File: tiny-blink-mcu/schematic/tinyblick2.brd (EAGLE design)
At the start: 35 x 35 mm, 57 parts, among them IC1 SE555D, IC2 LM358D, IC3 74LS595D, IC4 74LS595D, J1 USB-MICROB

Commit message: Updated schematic and board layout
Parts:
- removed C3: 10nF, adafruit:C0603
- removed C4: 100nF, adafruit:C0603
- removed C6: 5nF, adafruit:C0603
- removed C7: 0uF, adafruit:C0603
- removed C9: 4.7uF, adafruit:C0603
- removed IC1: SE555D, adafruit:SO08
- removed IC2: LM358D, linear:SO08
- removed R10: 10K, adafruit:R0603
- removed R11: 1K, adafruit:R0603
- removed R12: 5.1K, adafruit:R0603
- added C12: 10nF, adafruit:C0603
- added S1: MOMENTARY-SWITCH-SPST-SMD-4.6X2.8MM, SparkFun-Switches:TACTILE_SWITCH_SMD_4.6X2.8MM
- added TP1, TP2, TP3, TP4, TP5, TP6: TPB1,27, testpad:B1,27
- R1: value 10K -> (none)
- moved R1 13.6 mm to (6.50, 23.5), turned to 270 degrees
- moved C10 7.52 mm to (17.8, 31.3), turned to 180 degrees
- moved U$2 4.30 mm to (17.7, 27.7), turned to 270 degrees
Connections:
- removed net CLR: IC3.12, IC4.12, U$2.2
- removed net N$26: IC2.3, R1.1, R10.2
- removed net N$3: IC1.7, R11.1, R12.2
- removed net N$30: C6.2, IC1.5
- removed net N$6: C7.1, C9.1, IC1.2, IC1.6, R12.1
- new net LATCH: C12.2, IC3.12, IC4.12, TP1.TP, U$2.2
- new net NRES: TP3.TP, U$2.1
- new net PB4: R1.1, S1.3, S1.4, TP2.TP, U$2.3
- net +3V3: no longer C3.1, C4.1, IC1.4, IC1.8, IC2.8, R11.2
- net CLK: no longer IC1.3, IC2.2
- net GND: now also C12.1, S1.1, S1.2; no longer C3.2, C4.2, C6.1, C7.2, C9.2, IC1.1, IC2.4, R10.1
- net PWM: now also TP6.TP
- net RCLK: now also TP5.TP; no longer IC2.1
- net SER: now also TP4.TP
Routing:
- net +3V3: track 136.1 -> 80.0 mm
- net LATCH: track 0.00 -> 42.3 mm, vias 0 -> 2
- net PB4: track 0.00 -> 35.0 mm
- net GND: track 125.9 -> 96.3 mm, vias 11 -> 8
- net CLR: track 24.7 -> 0.00 mm, vias 2 -> 0
- net CLK: track 28.1 -> 8.74 mm, vias 3 -> 1
- net N$6: track 18.5 -> 0.00 mm
- net SER: track 9.80 -> 25.8 mm
- net N$26: track 9.10 -> 0.00 mm, vias 2 -> 0
- net PWM: track 30.9 -> 23.9 mm, vias 5 -> 3
- net RCLK: track 14.3 -> 9.17 mm, vias 2 -> 0
- net N$3: track 4.16 -> 0.00 mm
- net NRES: track 0.00 -> 3.55 mm
- net N$30: track 2.14 -> 0.00 mm

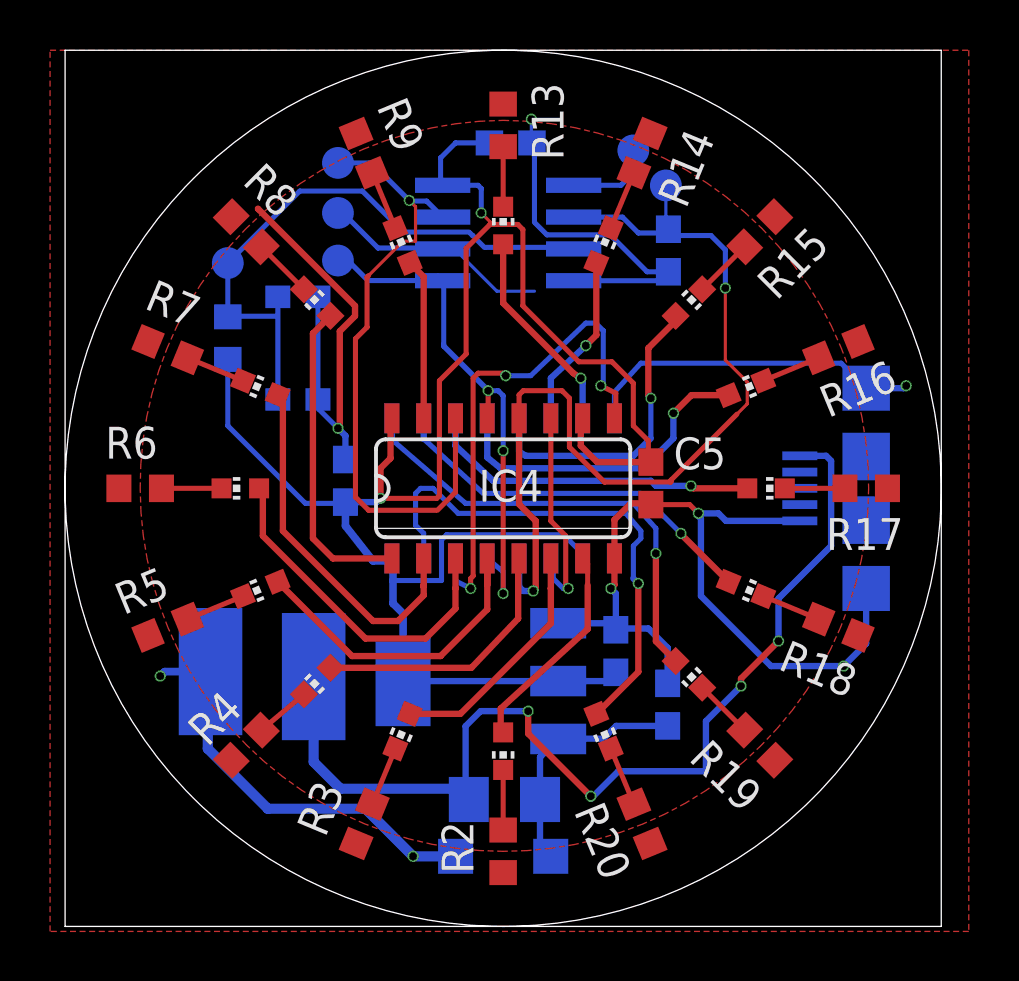
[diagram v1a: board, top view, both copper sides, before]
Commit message: Fixed RCLK trace missing issue
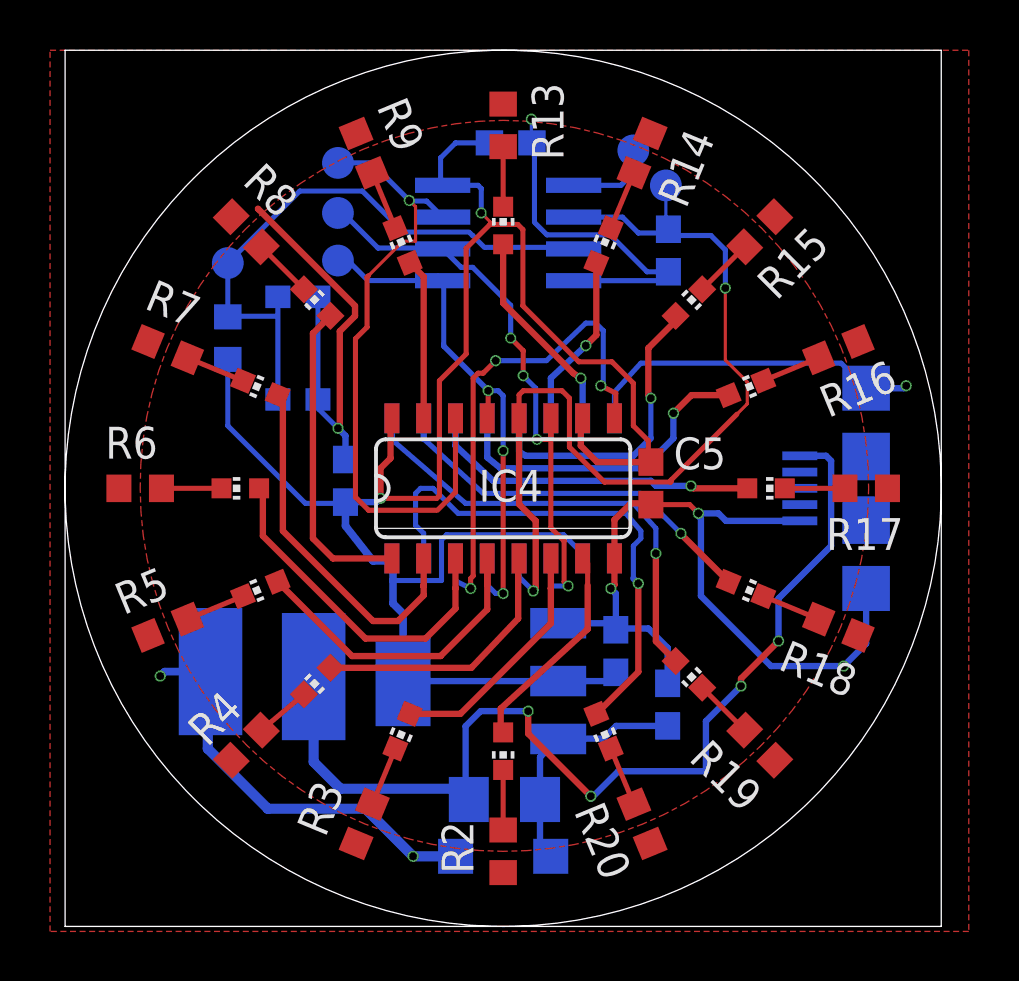
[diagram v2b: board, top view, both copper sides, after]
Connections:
- removed net CLK: IC3.11, IC4.11
- net RCLK: now also IC3.11, IC4.11
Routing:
- net RCLK: track 9.17 -> 25.0 mm, vias 0 -> 4
- net CLK: track 8.74 -> 0.00 mm, vias 1 -> 0
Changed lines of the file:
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@@
 <contactref element="TP5" pad="TP"/>
 <wire x1="15" y1="27.125" x2="15.0838" y2="27.065" width="0.127" layer="16"/>
-<wire x1="17.25" y1="25.375" x2="18.75" y2="25.375" width="0.127" layer="16"/>
-<wire x1="15.625" y1="27" x2="17.25" y2="25.375" width="0.127" layer="16"/>
 <wire x1="15.125" y1="27" x2="15.625" y2="27" width="0.127" layer="16"/>
 <wire x1="15.125" y1="27" x2="15.0838" y2="27.065" width="0.127" layer="16"/>
@@
 <wire x1="12.5" y1="27.1" x2="14.975" y2="27.1" width="0.2032" layer="16"/>
 <wire x1="14.975" y1="27.1" x2="15" y2="27.125" width="0.2032" layer="16"/>
-</signal>
-<signal name="CLK">
+<contactref element="IC3" pad="11"/>
 <contactref element="IC4" pad="11"/>
-<contactref element="IC3" pad="11"/>
-<wire x1="19.405" y1="20.3" x2="19.405" y2="16.195" width="0.2032" layer="1"/>
-<wire x1="19.405" y1="16.195" x2="20" y2="15.6" width="0.2032" layer="1"/>
-<wire x1="20" y1="15.6" x2="20" y2="13.6" width="0.2032" layer="1"/>
-<wire x1="20" y1="13.6" x2="20.1" y2="13.5" width="0.2032" layer="1"/>
-<via x="20.1" y="13.5" extent="1-16" drill="0.3048"/>
-<wire x1="20.1" y1="13.5" x2="19.9" y2="13.5" width="0.2032" layer="16"/>
-<wire x1="19.9" y1="13.5" x2="19.5" y2="13.9" width="0.2032" layer="16"/>
-<wire x1="19.5" y1="13.9" x2="19.5" y2="14.695" width="0.2032" layer="16"/>
-<wire x1="19.5" y1="14.695" x2="19.405" y2="14.7" width="0.2032" layer="16"/>
+<wire x1="15.0838" y1="27.065" x2="15.8204" y2="26.3284" width="0.2032" layer="16"/>
+<wire x1="15.8204" y1="26.3284" x2="16.2833875" y2="26.3284" width="0.2032" layer="16"/>
+<via x="17.8" y="23.5" extent="1-16" drill="0.3"/>
+<wire x1="17.8" y1="23.5" x2="18.3" y2="23" width="0.2032" layer="1"/>
+<wire x1="18.3" y1="23" x2="18.3" y2="22" width="0.2032" layer="1"/>
+<via x="18.3" y="22" extent="1-16" drill="0.3"/>
+<wire x1="18.3" y1="22" x2="18.8" y2="21.5" width="0.2032" layer="16"/>
+<wire x1="18.8" y1="19.5055" x2="18.85275" y2="19.45275" width="0.2032" layer="16"/>
+<via x="18.85275" y="19.45275" extent="1-16" drill="0.3"/>
+<wire x1="18.85275" y1="19.45275" x2="19.35275" y2="19.45275" width="0.2032" layer="1"/>
+<wire x1="19.405" y1="19.505" x2="19.405" y2="20.3" width="0.2032" layer="1"/>
+<wire x1="18.8" y1="21.5" x2="18.8" y2="19.5055" width="0.2032" layer="16"/>
+<wire x1="19.35275" y1="19.45275" x2="19.405" y2="19.505" width="0.2032" layer="1"/>
+<wire x1="17.8" y1="24.8117875" x2="17.8" y2="23.5" width="0.2032" layer="16"/>
+<wire x1="16.2833875" y1="26.3284" x2="17.8" y2="24.8117875" width="0.2032" layer="16"/>
+<wire x1="19.405" y1="20.3" x2="19.405" y2="15.9232875" width="0.2032" layer="1"/>
+<wire x1="19.9336" y1="13.7664" x2="20.1" y2="13.6" width="0.2032" layer="1"/>
+<wire x1="19.405" y1="15.9232875" x2="19.9336" y2="15.3946875" width="0.2032" layer="1"/>
+<wire x1="19.9336" y1="15.3946875" x2="19.9336" y2="13.7664" width="0.2032" layer="1"/>
+<via x="20.1" y="13.6" extent="1-16" drill="0.3"/>
+<wire x1="20.1" y1="13.6" x2="19.4" y2="13.6" width="0.2032" layer="16"/>
+<wire x1="19.4" y1="13.6" x2="19.4" y2="14.695" width="0.2032" layer="16"/>
+<wire x1="19.4" y1="14.695" x2="19.405" y2="14.7" width="0.2032" layer="16"/>
 </signal>
 <signal name="N$27">
@@
 <wire x1="16.2" y1="13.5" x2="16.2" y2="13.9" width="0.2032" layer="1"/>
 <wire x1="16.2" y1="13.9" x2="16.3" y2="14" width="0.2032" layer="1"/>
-<via x="17.6" y="22" extent="1-16" drill="0.3048"/>
+<via x="17.2" y="22.6" extent="1-16" drill="0.3048"/>
 <wire x1="20.8" y1="24.1" x2="21.2" y2="24.1" width="0.2032" layer="16"/>
 <wire x1="21.2" y1="24.1" x2="21.5" y2="23.8" width="0.2032" layer="16"/>
@@
 <wire x1="22" y1="21.3" x2="22" y2="20.355" width="0.2032" layer="1"/>
 <wire x1="22" y1="20.355" x2="21.945" y2="20.3" width="0.2032" layer="1"/>
-<wire x1="20.8" y1="24.1" x2="18.6" y2="22" width="0.2032" layer="16"/>
-<wire x1="18.6" y1="22" x2="17.6" y2="22" width="0.2032" layer="16"/>
+<wire x1="20.8" y1="24.1" x2="19.228571875" y2="22.6" width="0.2032" layer="16"/>
+<wire x1="19.228571875" y1="22.6" x2="17.2" y2="22.6" width="0.2032" layer="16"/>
 <wire x1="16.3" y1="21.9" x2="16.5" y2="22.1" width="0.2032" layer="1"/>
-<wire x1="16.5" y1="22.1" x2="17.5" y2="22.1" width="0.2032" layer="1"/>
-<wire x1="17.5" y1="22.1" x2="17.6" y2="22" width="0.2032" layer="1"/>
+<wire x1="16.5" y1="22.1" x2="16.7" y2="22.1" width="0.2032" layer="1"/>
+<wire x1="16.7" y1="22.1" x2="17.2" y2="22.6" width="0.2032" layer="1"/>
 <wire x1="16.3" y1="14" x2="16.3" y2="21.9" width="0.2032" layer="1"/>
 </signal>
@@
 <wire x1="18.8" y1="13.5" x2="18.7" y2="13.4" width="0.254" layer="1"/>
 <via x="18.7" y="13.4" extent="1-16" drill="0.3048"/>
-<wire x1="18.7" y1="13.4" x2="18.3" y2="13.4" width="0.254" layer="16"/>
-<wire x1="18.3" y1="13.4" x2="18.1" y2="13.6" width="0.254" layer="16"/>
-<wire x1="18.1" y1="13.6" x2="18.135" y2="13.635" width="0.254" layer="16"/>
-<wire x1="18.135" y1="13.635" x2="18.135" y2="14.7" width="0.254" layer="16"/>
 <wire x1="18.235" y1="20.4" x2="18.135" y2="20.3" width="0.2032" layer="1"/>
 <contactref element="TP1" pad="TP"/>
@@
 <wire x1="24.2" y1="17.75" x2="24.2" y2="17.825" width="0.2032" layer="1"/>
 <wire x1="24.2" y1="17.825" x2="26.8375" y2="20.4625" width="0.2032" layer="1"/>
+<wire x1="18.135" y1="14.7" x2="18.135" y2="13.965" width="0.2032" layer="16"/>
+<wire x1="18.135" y1="13.965" x2="18.7" y2="13.4" width="0.2032" layer="16"/>
 </signal>
 <signal name="PWM">
@@
 <contactref element="IC3" pad="13"/>
 <via x="17.5" y="13.3" extent="1-16" drill="0.3048"/>
-<wire x1="17.5" y1="13.3" x2="17.5" y2="14.165" width="0.2032" layer="16"/>
-<wire x1="17.5" y1="14.165" x2="16.865" y2="14.7" width="0.2032" layer="16"/>
 <wire x1="17.5" y1="13.3" x2="17.5" y2="19" width="0.2032" layer="1"/>
 <via x="17.5" y="19" extent="1-16" drill="0.3048"/>
@@
 <wire x1="12.1" y1="25.8" x2="14.7" y2="25.8" width="0.2032" layer="16"/>
 <wire x1="14.7" y1="25.8" x2="14.8875" y2="25.9875" width="0.2032" layer="16"/>
+<wire x1="16.865" y1="14.7" x2="16.865" y2="13.635" width="0.2032" layer="16"/>
+<wire x1="17.2" y1="13.3" x2="17.5" y2="13.3" width="0.2032" layer="16"/>
+<wire x1="16.865" y1="13.635" x2="17.2" y2="13.3" width="0.2032" layer="16"/>
 </signal>
 <signal name="NRES">

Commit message: Minor board fixes and other changes
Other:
- outline, holes or cut-outs redrawn
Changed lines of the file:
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@@
 <drawing>
 <settings>
-<setting alwaysvectorfont="no"/>
+<setting alwaysvectorfont="yes"/>
 <setting keepoldvectorfont="yes"/>
 <setting verticaltext="up"/>
@@
 <grid distance="0.1" unitdist="mm" unit="mm" style="lines" multiple="1" display="no" altdistance="5" altunitdist="mil" altunit="mil"/>
 <layers>
-<layer number="1" name="Top" color="4" fill="1" visible="no" active="yes"/>
+<layer number="1" name="Top" color="4" fill="1" visible="yes" active="yes"/>
 <layer number="16" name="Bottom" color="1" fill="1" visible="yes" active="yes"/>
 <layer number="17" name="Pads" color="2" fill="1" visible="yes" active="yes"/>
@@
 <layer number="19" name="Unrouted" color="6" fill="1" visible="yes" active="yes"/>
 <layer number="20" name="Dimension" color="15" fill="1" visible="yes" active="yes"/>
-<layer number="21" name="tPlace" color="7" fill="1" visible="no" active="yes"/>
+<layer number="21" name="tPlace" color="7" fill="1" visible="yes" active="yes"/>
 <layer number="22" name="bPlace" color="7" fill="1" visible="yes" active="yes"/>
-<layer number="23" name="tOrigins" color="15" fill="1" visible="no" active="yes"/>
+<layer number="23" name="tOrigins" color="15" fill="1" visible="yes" active="yes"/>
 <layer number="24" name="bOrigins" color="15" fill="1" visible="yes" active="yes"/>
-<layer number="25" name="tNames" color="7" fill="1" visible="no" active="yes"/>
+<layer number="25" name="tNames" color="7" fill="1" visible="yes" active="yes"/>
 <layer number="26" name="bNames" color="7" fill="1" visible="yes" active="yes"/>
 <layer number="27" name="tValues" color="7" fill="1" visible="no" active="yes"/>
@@
 <layer number="37" name="tTest" color="7" fill="1" visible="no" active="yes"/>
 <layer number="38" name="bTest" color="7" fill="1" visible="no" active="yes"/>
-<layer number="39" name="tKeepout" color="4" fill="11" visible="no" active="yes"/>
+<layer number="39" name="tKeepout" color="4" fill="11" visible="yes" active="yes"/>
 <layer number="40" name="bKeepout" color="1" fill="11" visible="yes" active="yes"/>
-<layer number="41" name="tRestrict" color="4" fill="10" visible="no" active="yes"/>
+<layer number="41" name="tRestrict" color="4" fill="10" visible="yes" active="yes"/>
 <layer number="42" name="bRestrict" color="1" fill="10" visible="yes" active="yes"/>
 <layer number="43" name="vRestrict" color="2" fill="10" visible="no" active="yes"/>
@@
 <layer number="49" name="Reference" color="7" fill="1" visible="no" active="yes"/>
 <layer number="50" name="dxf" color="7" fill="1" visible="no" active="no"/>
-<layer number="51" name="tDocu" color="7" fill="1" visible="no" active="yes"/>
+<layer number="51" name="tDocu" color="7" fill="1" visible="yes" active="yes"/>
 <layer number="52" name="bDocu" color="7" fill="1" visible="yes" active="yes"/>
 <layer number="53" name="tGND_GNDA" color="7" fill="9" visible="no" active="no"/>
@@
 <board>
 <plain>
-<wire x1="0" y1="0" x2="35" y2="0" width="0" layer="20"/>
-<wire x1="35" y1="0" x2="35" y2="35" width="0" layer="20"/>
-<wire x1="35" y1="35" x2="0" y2="35" width="0" layer="20"/>
-<wire x1="0" y1="35" x2="0" y2="0" width="0" layer="20"/>
 <circle x="17.5" y="17.5" radius="17.5" width="0.015240625" layer="20"/>
 <text x="32.3" y="22.9" size="1.778" layer="22" rot="MR0">TB2.0a0</text>
@@
 </class>
 </classes>
-<designrules name="jlcpcb-2layers">
+<designrules name="jlcpcb-2layers *">
 <description language="en">&lt;b&gt;JLCPCB design rules (2 layers)&lt;/b&gt;
 &lt;ul&gt;
@@
 <param name="mlMinCreamFrame" value="0mil"/>
 <param name="mlMaxCreamFrame" value="0mil"/>
-<param name="mlViaStopLimit" value="0mil"/>
+<param name="mlViaStopLimit" value="14mil"/>
 <param name="srRoundness" value="0"/>
 <param name="srMinRoundness" value="0mil"/>
@@
 <wire x1="18.75" y1="28.125" x2="18.75" y2="31.2" width="0.2032" layer="16"/>
 <wire x1="10.1" y1="25.15" x2="10.1" y2="21.05" width="0.2032" layer="16"/>
-<wire x1="24.1" y1="26.15" x2="28.351040625" y2="28.351040625" width="0" layer="19" extent="1-16"/>
-<wire x1="17.5" y1="32.85" x2="18.626059375" y2="32.395175" width="0" layer="19" extent="1-1"/>
-<wire x1="23.373278125" y1="31.675296875" x2="18.65" y2="31.3" width="0" layer="19" extent="1-16"/>
-<wire x1="22.045" y1="20.4" x2="20.875" y2="25.875" width="0" layer="19" extent="16-16"/>
-<wire x1="31.675296875" y1="23.365278125" x2="32" y2="21.5" width="0" layer="19" extent="1-16"/>
-<wire x1="23.4" y1="16.85" x2="21.945" y2="20.3" width="0" layer="19" extent="1-16"/>
-<wire x1="31.675296875" y1="11.62471875" x2="31.1" y2="10.4" width="0" layer="19" extent="1-1"/>
-<wire x1="32.85" y1="17.1465125" x2="29.35" y2="16.2" width="0" layer="19" extent="1-16"/>
-<wire x1="28.351040625" y1="6.63895625" x2="31.1" y2="10.4" width="0" layer="19" extent="1-1"/>
-<wire x1="23.373278125" y1="3.3147" x2="28.351040625" y2="6.63895625" width="0" layer="19" extent="1-1"/>
-<wire x1="17.5" y1="2.15" x2="23.373278125" y2="3.3147" width="0" layer="19" extent="1-1"/>
-<wire x1="15.6" y1="2.8" x2="17.5" y2="2.15" width="0" layer="19" extent="1-16"/>
-<wire x1="3.3147" y1="11.62471875" x2="3.8" y2="10" width="0" layer="19" extent="1-1"/>
-<wire x1="11.62471875" y1="3.3147" x2="13.9" y2="2.8" width="0" layer="19" extent="1-1"/>
-<wire x1="6.63895625" y1="6.63895625" x2="5.81" y2="10.18" width="0" layer="19" extent="1-16"/>
-<wire x1="2.15" y1="17.5" x2="3.3147" y2="11.62471875" width="0" layer="19" extent="1-1"/>
-<wire x1="3.3147" y1="23.365278125" x2="2.15" y2="17.5" width="0" layer="19" extent="1-1"/>
-<wire x1="11.62471875" y1="31.675296875" x2="17.5" y2="32.85" width="0" layer="19" extent="1-1"/>
-<wire x1="7.701675" y1="28.673184375" x2="11.62471875" y2="31.675296875" width="0" layer="19" extent="1-1"/>
-<wire x1="6.63895625" y1="28.351040625" x2="7.701675" y2="28.673184375" width="0" layer="19" extent="1-1"/>
 </signal>
 <signal name="VCC">
@@
 <contactref element="IC4" pad="2"/>
 <wire x1="14.325" y1="14.7" x2="14.325" y2="13.625" width="0.254" layer="1"/>
-<wire x1="14.325" y1="13.625" x2="14.3" y2="13.6" width="0.254" layer="1"/>
 <wire x1="14.325" y1="13.625" x2="14.325" y2="13.225" width="0.254" layer="1"/>
 <wire x1="14.325" y1="13.225" x2="13.3" y2="12.2" width="0.254" layer="1"/>
@@
 <contactref element="TP5" pad="TP"/>
 <wire x1="15" y1="27.125" x2="15.0838" y2="27.065" width="0.127" layer="16"/>
-<wire x1="15.125" y1="27" x2="15.625" y2="27" width="0.127" layer="16"/>
 <wire x1="15.125" y1="27" x2="15.0838" y2="27.065" width="0.127" layer="16"/>
 <wire x1="10.9" y1="28.5" x2="11.1" y2="28.5" width="0.2032" layer="16"/>
@@
 <wire x1="13" y1="20.245" x2="13.055" y2="20.3" width="0.254" layer="1"/>
 <contactref element="IC3" pad="10"/>
-<wire x1="20.675" y1="20.3" x2="20.7" y2="20.325" width="0.2032" layer="1"/>
 <wire x1="20.7264" y1="14.8336" x2="20.675" y2="14.7" width="0.254" layer="16"/>
 <wire x1="23.4" y1="18.55" x2="21.25" y2="18.55" width="0.254" layer="1"/>
@@
 <wire x1="22.7" y1="18.8" x2="23.4" y2="19.5" width="0.254" layer="16"/>
 <wire x1="23.4" y1="19.5" x2="23.4" y2="21.1" width="0.2032" layer="16"/>
-<wire x1="23.4" y1="21.1" x2="23.4" y2="21.2" width="0.254" layer="16"/>
 <via x="23.4" y="21.1" extent="1-16" drill="0.3048"/>
 <wire x1="24.38966875" y1="24.38966875" x2="24.38966875" y2="24.18966875" width="0.254" layer="1"/>

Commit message: Removed unused files, update board, code and other changes
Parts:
- removed TP1, TP2, TP3, TP4, TP5, TP6: TPB1,27, testpad:B1,27
- added LED17: (no value), led:CHIP-LED0603
- added R10: (no value), adafruit:R0603
- renumbered VCC to 5V
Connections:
- new net N$2: LED17.C, R10.2
- net GND: now also R10.1
- net LATCH: no longer TP1.TP
- net NRES: now also LED17.A; no longer TP3.TP
- net PB4: no longer TP2.TP
- net PWM: no longer TP6.TP
- net RCLK: no longer TP5.TP
- net SER: no longer TP4.TP
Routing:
- net LATCH: track 42.1 -> 36.5 mm
- net PB4: track 35.0 -> 29.9 mm
- net PWM: track 24.1 -> 19.5 mm
- net N$2: track 0.00 -> 3.96 mm
- net N$54: track 20.8 -> 17.6 mm
- net SER: track 25.8 -> 23.1 mm, vias 1 -> 3
- net RCLK: track 24.5 -> 21.8 mm
- net N$18: track 14.5 -> 12.5 mm
- net +3V3: track 80.0 -> 78.1 mm, vias 2 -> 4
- net N$34: track 13.5 -> 11.7 mm
- net GND: track 96.3 -> 97.5 mm
- net NRES: track 3.55 -> 2.74 mm
- net N$29: track 10.8 -> 10.2 mm
